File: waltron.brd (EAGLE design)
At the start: 53.6 x 47 mm, 25 parts, among them IC1 4049N, U1 LM386

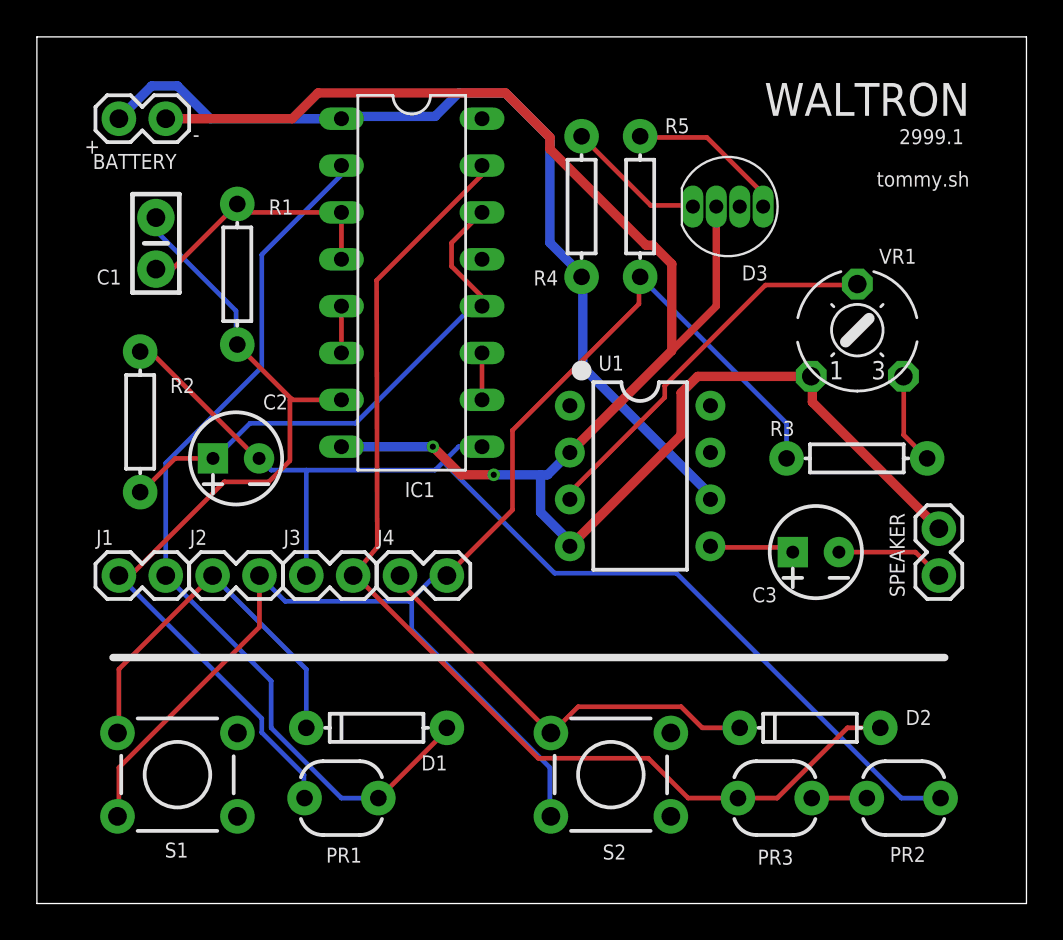
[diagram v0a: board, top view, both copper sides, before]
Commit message: Re-routed, missing D3 GND
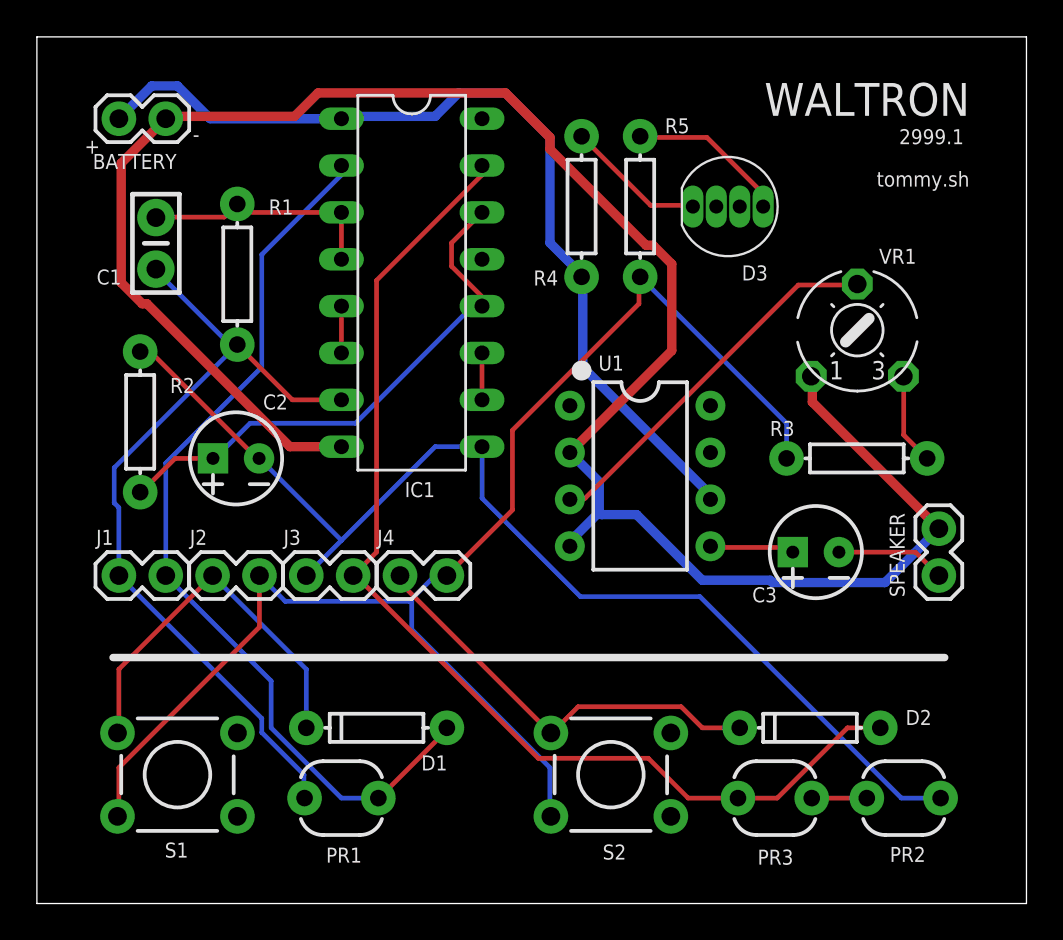
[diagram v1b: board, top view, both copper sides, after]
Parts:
- turned C1 to 90 degrees
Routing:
- net GND: track 101.0 -> 109.0 mm, vias 2 -> 0
- net N$3: track 47.1 -> 44.8 mm
- net N$2: track 14.3 -> 13.1 mm
- net N$16: track 21.0 -> 20.4 mm

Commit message: Replaced D3 component w/ spaced leads
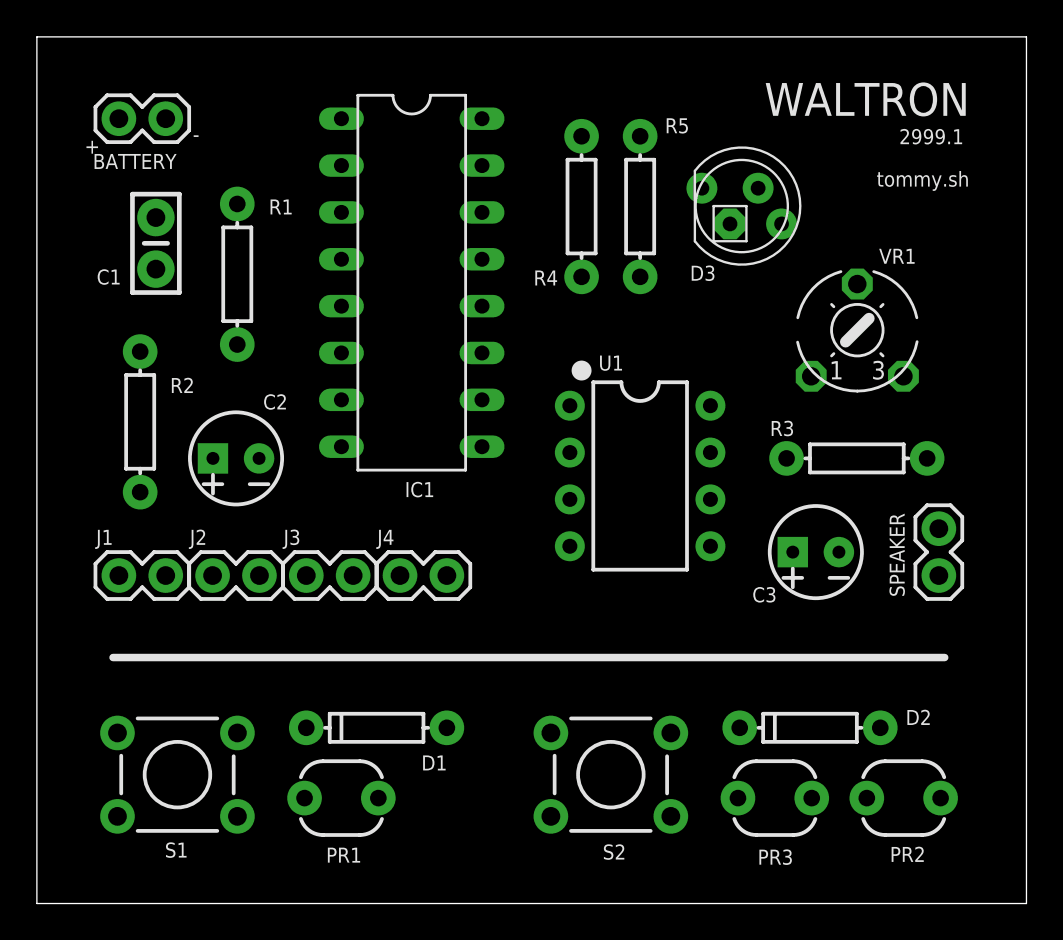
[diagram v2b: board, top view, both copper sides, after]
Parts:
- D3: value RGB LED -> 5MMRGBLED; device SparkFun-LED:LED-RGB-THRU -> adafruit:LED5MMRGB
- moved D3 0.74 mm to (38.2, 37.8), turned to 0 degrees
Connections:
- net GND: now also D3.3; no longer D3.2
- net N$17: now also D3.1; no longer D3.4
- net N$18: now also D3.4; no longer D3.1
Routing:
- net GND: track 109.0 -> 0.00 mm
- net N$12: track 76.1 -> 0.00 mm
- net N$5: track 61.9 -> 0.00 mm
- net N$8: track 60.3 -> 0.00 mm
- net V+: track 49.6 -> 0.00 mm
- net N$4: track 49.5 -> 0.00 mm
- net N$3: track 44.8 -> 0.00 mm
- net N$7: track 29.1 -> 0.00 mm
- net N$11: track 23.2 -> 0.00 mm
- net N$9: track 21.1 -> 0.00 mm
- net N$16: track 20.4 -> 0.00 mm
- net N$2: track 13.1 -> 0.00 mm
- net N$17: track 8.65 -> 0.00 mm
- net N$18: track 7.65 -> 0.00 mm
- net N$15: track 5.94 -> 0.00 mm
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
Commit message: Autorouted -- NO DRC ERRORS!
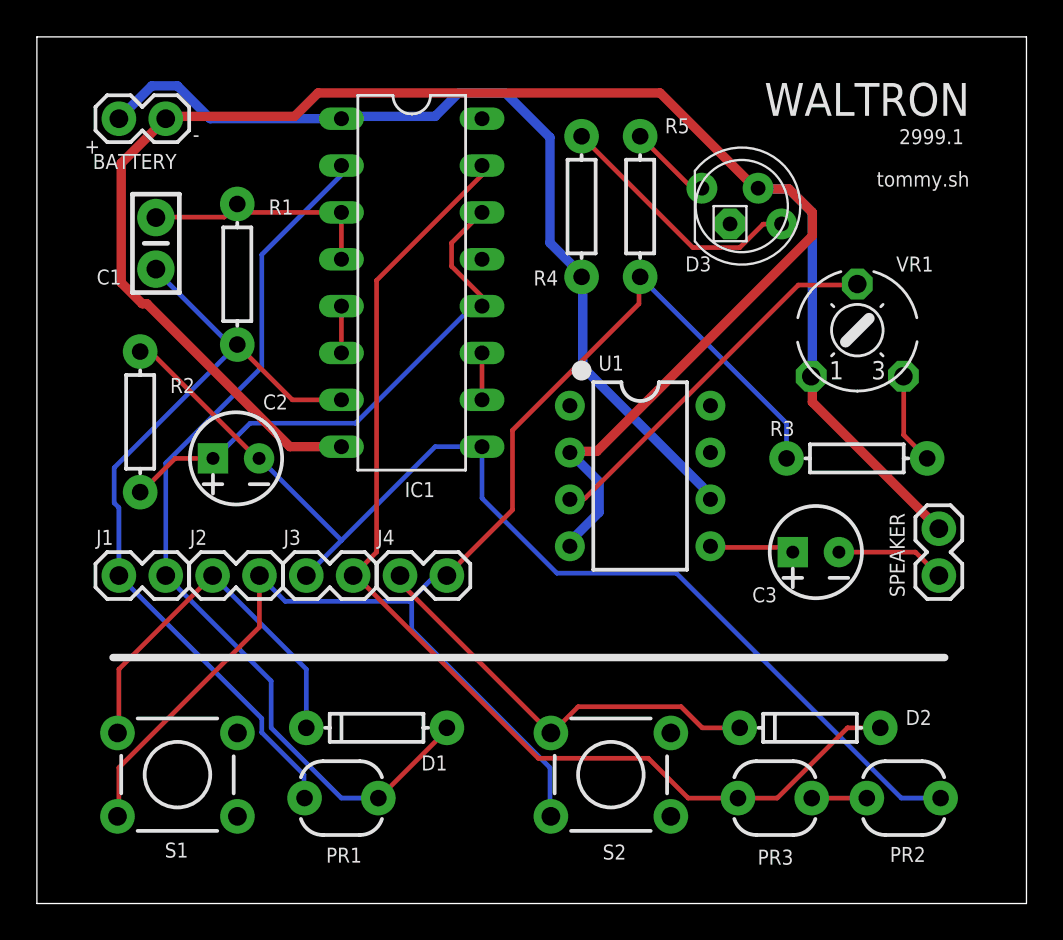
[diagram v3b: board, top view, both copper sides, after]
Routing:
- net GND: track 0.00 -> 113.0 mm
- net N$12: track 0.00 -> 76.1 mm
- net N$5: track 0.00 -> 61.9 mm
- net N$8: track 0.00 -> 60.3 mm
- net V+: track 0.00 -> 49.6 mm
- net N$4: track 0.00 -> 49.5 mm
- net N$3: track 0.00 -> 44.8 mm
- net N$7: track 0.00 -> 29.1 mm
- net N$11: track 0.00 -> 23.2 mm
- net N$9: track 0.00 -> 21.1 mm
- net N$16: track 0.00 -> 20.4 mm
- net N$18: track 0.00 -> 13.9 mm
- net N$2: track 0.00 -> 13.1 mm
- net N$15: track 0.00 -> 5.94 mm
- net N$13: track 0.00 -> 4.99 mm
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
